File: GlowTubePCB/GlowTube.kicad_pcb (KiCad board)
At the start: 2 copper layers, 80.5 x 92.2 mm, 43 parts, among them J1 Conn_01x07, P1 Solder_Pad, P2 Solder_Pad, P3 Solder_Pad, P4 Solder_Pad, P5 Solder_Pad, P6 Solder_Pad, SW1 TS-1185EC-C-D-B, SW2 TS-1185EC-C-D-B, U1 SN74LVC2T45DCUR, U2 ESP32-WROOM-32E, U3 CP2102-GMR, U4 BL1117-33CX, U5 UMH3N, U6 MSM261D4030H1CPM, U7 SS54

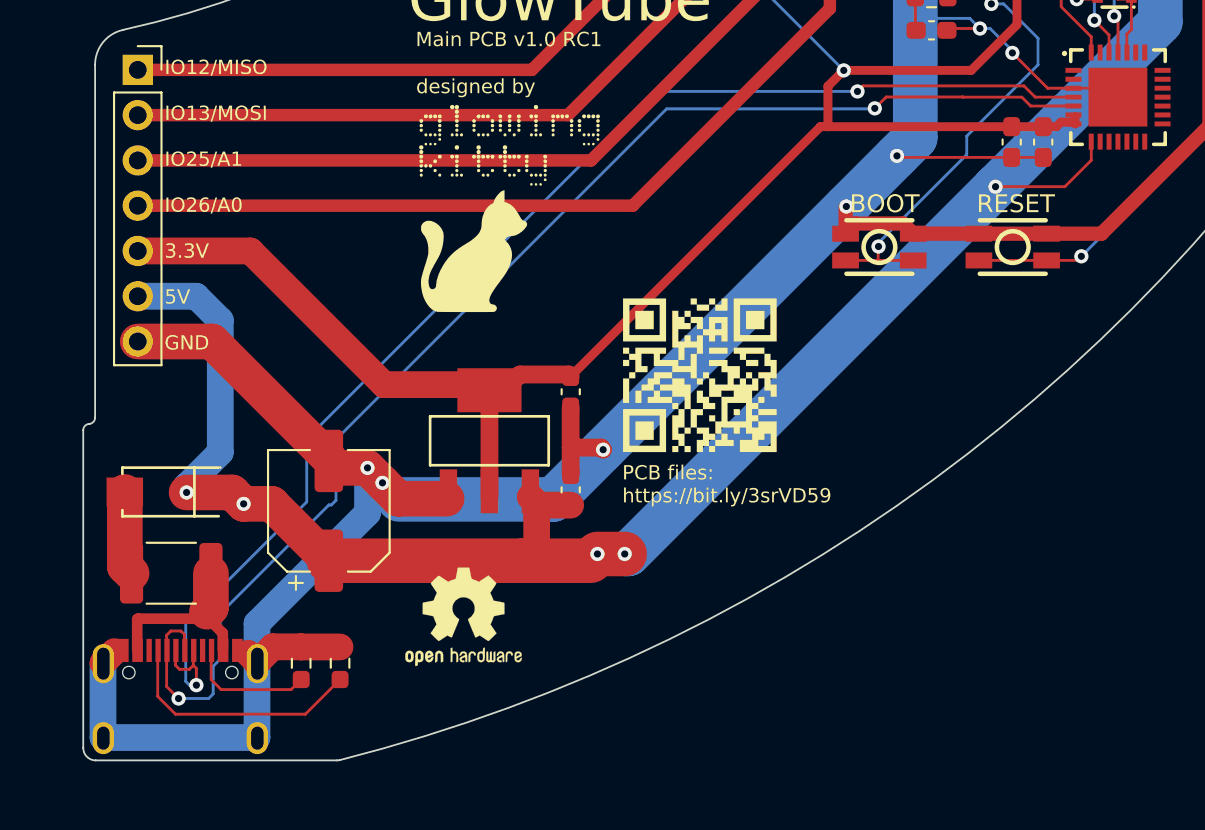
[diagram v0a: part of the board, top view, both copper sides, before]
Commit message: added second schottky diode for less heat
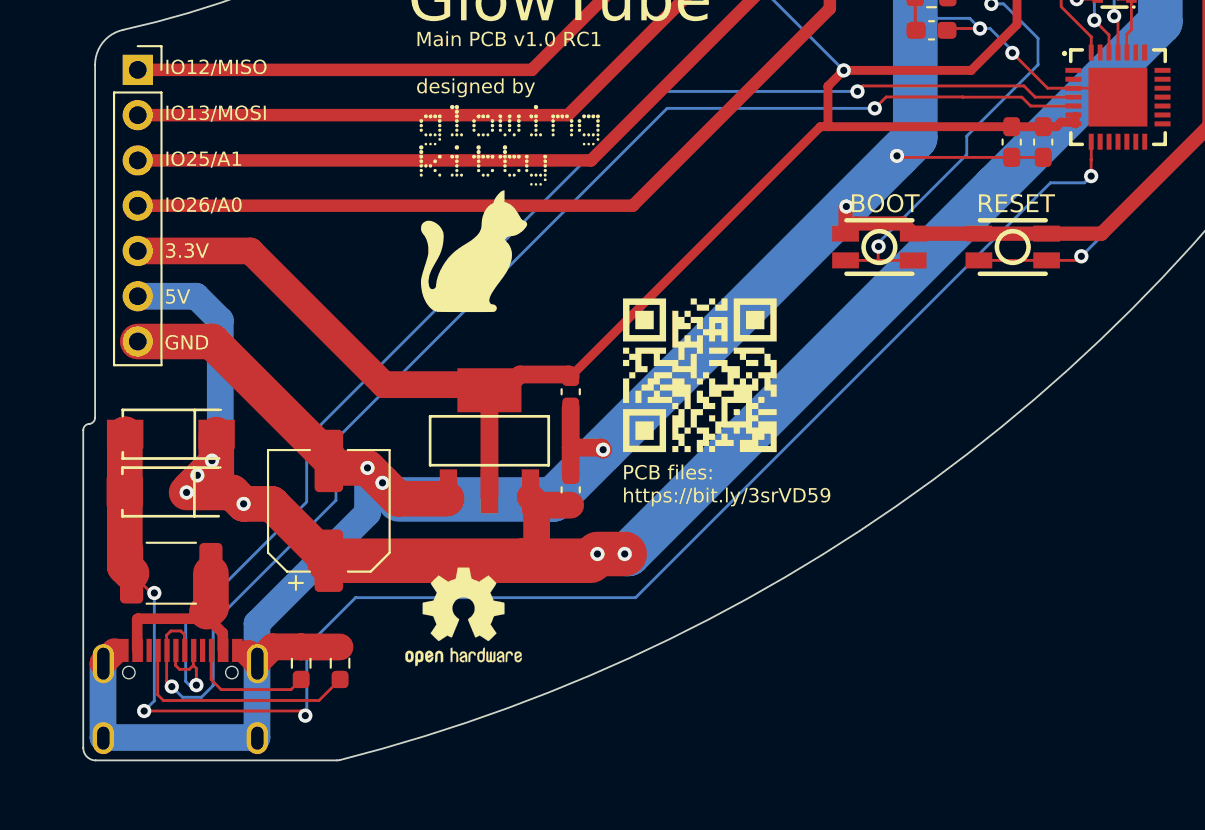
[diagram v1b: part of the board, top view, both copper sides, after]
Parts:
- added U8: SS54, footprint:SMA_L4.4-W2.8-LS5.4-RD, F.Cu at (91.4, 156.4)
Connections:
- F1 pad 1: VBUS -> Net-(USB1-PadA4B9)
- F1 pad 2: Net-(F1-Pad2) -> VBUS
- U3 pad 8: +5V -> VBUS
- U7 pad 2: Net-(F1-Pad2) -> VBUS
- USB1 pad A4B9: VBUS -> Net-(USB1-PadA4B9)
- USB1 pad B4A9: VBUS -> Net-(USB1-PadA4B9)
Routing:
- net VBUS: track 10.1 -> 87.1 mm, vias 0 -> 4
- net Net-(USB1-PadA4B9): track 0.00 -> 10.1 mm
- net Net-(F1-Pad2): track 5.15 -> 0.00 mm
- net +5V: track 170.7 -> 169.2 mm, vias 8 -> 9
- net USB-C CC1: track 14.1 -> 13.4 mm
- net USB-C DATA-: track 74.8 -> 74.2 mm

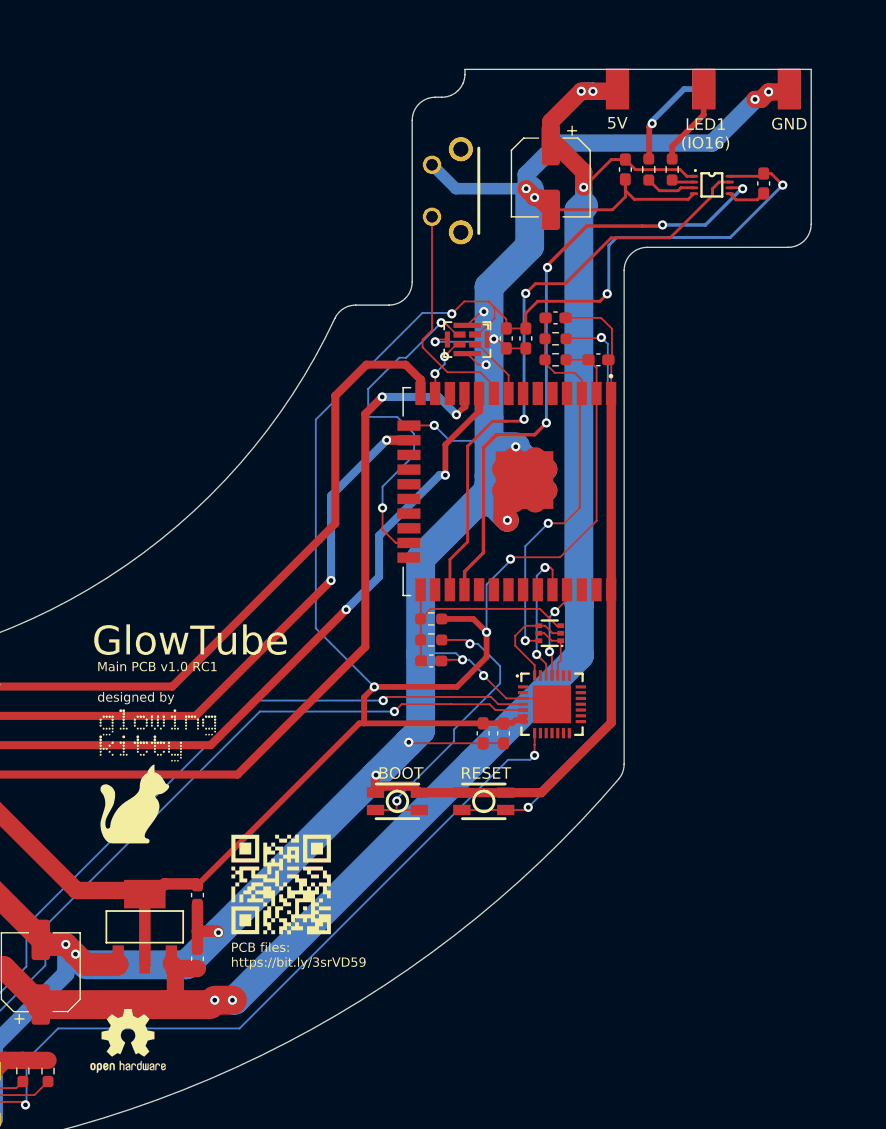
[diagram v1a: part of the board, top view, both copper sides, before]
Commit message: added option to disconnect leds from power
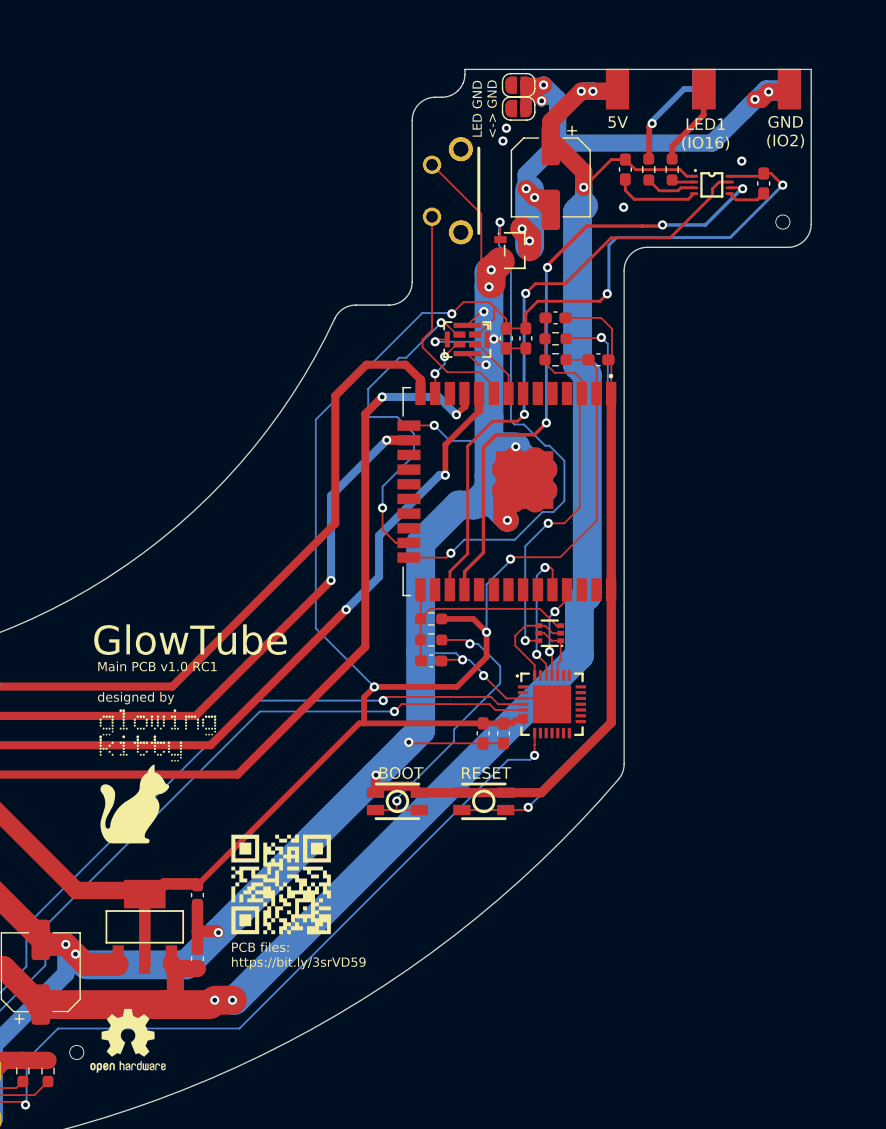
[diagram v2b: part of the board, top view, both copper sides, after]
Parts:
- added JP1: SolderJumper_2_Open, Jumper:SolderJumper-2_P1.3mm_Open_RoundedPad1.0x1.5mm, F.Cu at (141.7, 83.9)
- added JP2: SolderJumper_2_Open, Jumper:SolderJumper-2_P1.3mm_Open_RoundedPad1.0x1.5mm, F.Cu at (141.7, 85.9)
- added U9: AO3400A, footprint:SOT-23-3_L2.9-W1.6-P1.90-LS2.8-BR, F.Cu at (141.3, 98.2)
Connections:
- C4 pad 2: GND -> LED GND
- P3 pad 1: GND -> LED GND
- P5 pad 1: GND -> LED GND
- U2 pad 12: IO27 -> unconnected-(U2-Pad12)
- U2 pad 24: IO2 -> IO2/LEDPOWER
- U2 pad 26: IO4/A5 -> unconnected-(U2-Pad26)
- U2 pad 29: IO5 -> unconnected-(U2-Pad29)
- U2 pad 30: IO18 -> unconnected-(U2-Pad30)
- U2 pad 31: IO19 -> unconnected-(U2-Pad31)
- U2 pad 33: IO21 -> unconnected-(U2-Pad33)
- U2 pad 36: IO22 -> unconnected-(U2-Pad36)
- U2 pad 37: IO23 -> unconnected-(U2-Pad37)
- U2 pad 4: IO36/A4/SENSOR_VP -> unconnected-(U2-Pad4)
- U2 pad 5: I39/A3/SENSOR_VN -> unconnected-(U2-Pad5)
- U2 pad 6: I34/A2 -> unconnected-(U2-Pad6)
- U2 pad 7: IO35 -> unconnected-(U2-Pad7)
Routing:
- net LED GND: track 0.00 -> 56.4 mm, vias 0 -> 8
- net IO2/LEDPOWER: track 0.00 -> 44.3 mm, vias 0 -> 2
- net GND: track 356.2 -> 314.7 mm, vias 18 -> 20
- net +5V: track 169.2 -> 169.9 mm
- net (no net): vias 0 -> 2
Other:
- board text added: "GND (IO2)"
- board text added: "LED GND <-> GND"
- board text removed: "GND"

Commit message: updated pcbs
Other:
- board text added: "Main PCB v1.0"
- board text removed: "Main PCB v1.0 RC1"
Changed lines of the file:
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@@
     (effects (font (size 1 1) (thickness 0.15)) (justify mirror))
   )
-  (gr_text "Main PCB v1.0 RC1" (at 105.1284 134.2564) (layer "F.SilkS")
+  (gr_text "Main PCB v1.0" (at 105.1284 134.2564) (layer "F.SilkS")
     (effects (font (size 0.8 0.8) (thickness 0.15)) (justify left))
   )
@@
   (segment (start 98.94 172.19) (end 98.68 171.93) (width 0.16) (layer "F.Cu") (net 39))
   (segment (start 89.51 164.785) (end 89.205 164.48) (width 0.6) (layer "F.Cu") (net 39))
+  (segment (start 88.81462 163.81962) (end 88.81462 159.640025) (width 2) (layer "F.Cu") (net 39))
   (segment (start 143.034346 140.985654) (end 143.034346 141.035654) (width 0.16) (layer "F.Cu") (net 39))
-  (segment (start 88.81462 163.81962) (end 88.81462 159.640025) (width 2) (layer "F.Cu") (net 39))
   (segment (start 143.034346 139.889258) (end 143.034346 140.985654) (width 0.16) (layer "F.Cu") (net 39))
   (segment (start 143.03 140.99) (end 143.03 141.92) (width 0.16) (layer "F.Cu") (net 39))
